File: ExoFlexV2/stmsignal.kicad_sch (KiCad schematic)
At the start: 4 parts, among them J4 CN8, J5 CN9, J6 CN7, J7 CN10

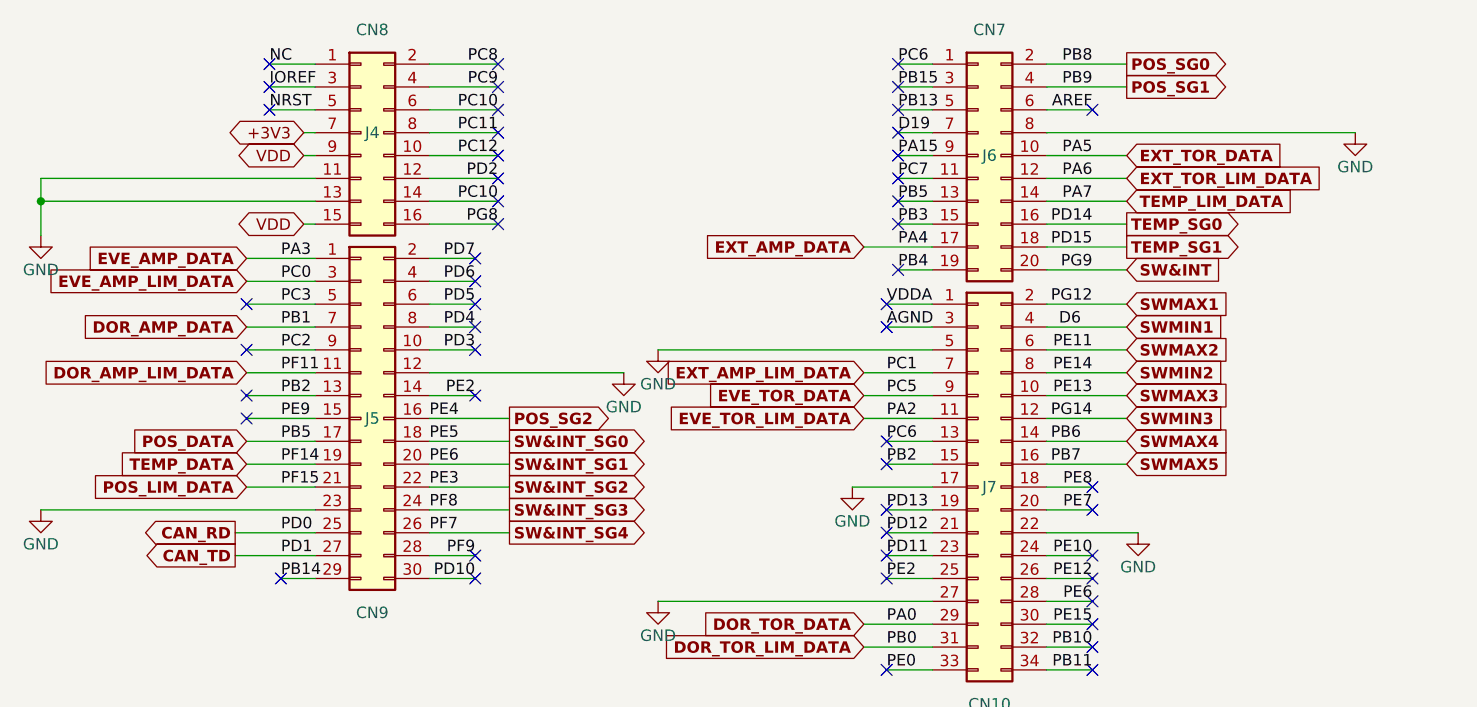
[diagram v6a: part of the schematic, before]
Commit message: Gestion de multiple signaux
- Ajout de multiplexeur 8:1 pour les signaux analogique supplémentaire
- Ajout de multiplexeur 8:1 arranger sous forme d'un 32:1
- Ajout du footprint pour le mux choisis
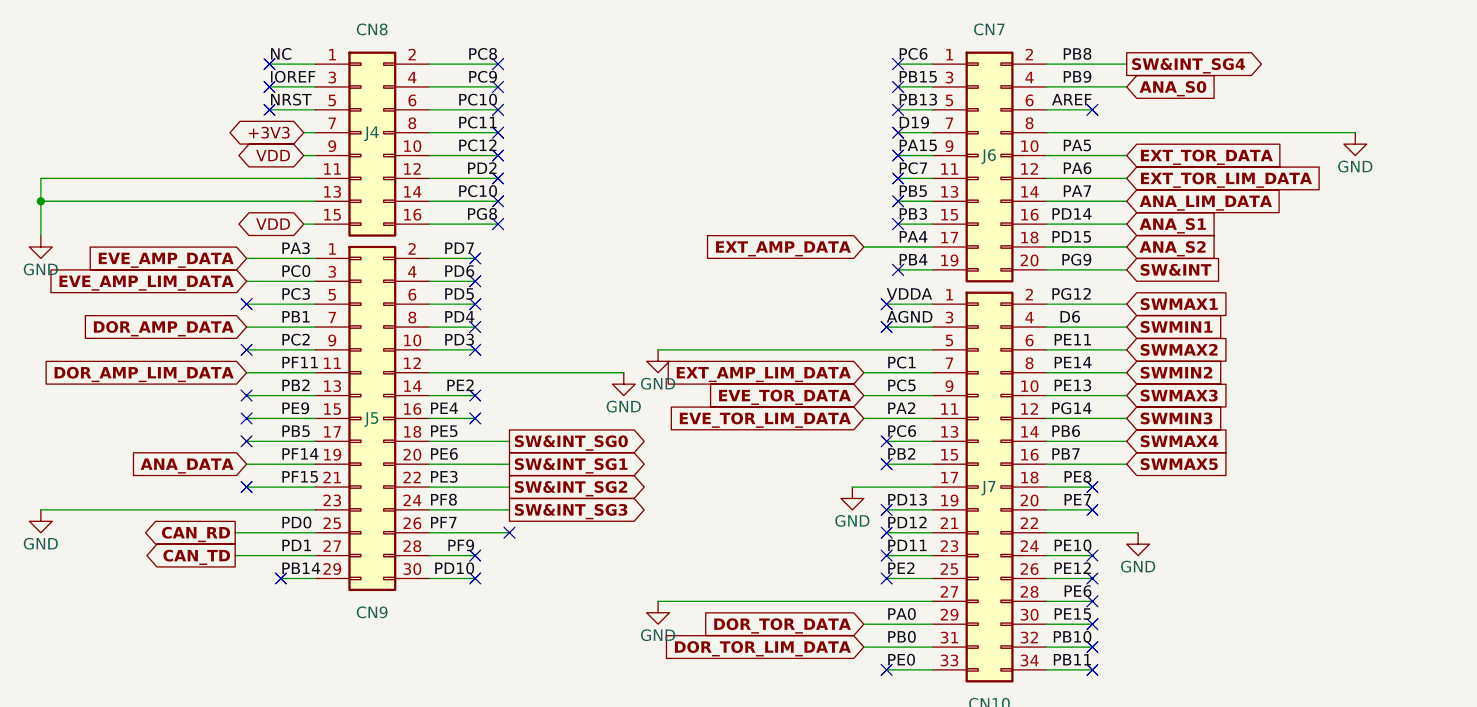
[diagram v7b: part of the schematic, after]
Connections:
- net POS_SG0 is gone; now on net SW&INT_SG4: J6.2 (Pin_2)
- net SW&INT_SG4: no longer J5.26 (Pin_26)
- net POS_DATA renamed PB5
- net POS_LIM_DATA renamed PF15
- net POS_SG1 renamed ANA_S0
- net POS_SG2 renamed PE4
- net TEMP_DATA renamed ANA_DATA
- net TEMP_LIM_DATA renamed ANA_LIM_DATA
- net TEMP_SG0 renamed ANA_S1
- net TEMP_SG1 renamed ANA_S2
- new net PF7: J5.26 (Pin_26)
- no-connect marks 51 -> 55
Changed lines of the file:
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@@
   )
   (no_connect (at 156.21 69.85))
+  (no_connect (at 83.82 101.6))
   (no_connect (at 111.76 67.31))
   (no_connect (at 86.36 54.61))
@@
   (no_connect (at 83.82 93.98))
   (no_connect (at 83.82 81.28))
+  (no_connect (at 109.22 93.98))
   (no_connect (at 111.76 54.61))
   (no_connect (at 177.8 116.84))
@@
   (no_connect (at 156.21 72.39))
   (no_connect (at 156.21 67.31))
+  (no_connect (at 113.03 106.68))
   (no_connect (at 156.21 64.77))
   (no_connect (at 154.94 109.22))
@@
   (no_connect (at 109.22 111.76))
   (no_connect (at 154.94 121.92))
+  (no_connect (at 83.82 96.52))
   (wire (pts (xy 152.4 93.98) (xy 160.02 93.98))
     (stroke (width 0.5) (type default) (color 40 35 255 1))
@@
     (stroke (width 0) (type default) (color 0 0 0 0))
   )
-  (wire (pts (xy 104.14 93.98) (xy 113.03 93.98))
-    (stroke (width 0.5) (type default) (color 255 74 249 1))
-  )
   (wire (pts (xy 86.36 57.15) (xy 91.44 57.15))
     (stroke (width 0) (type default) (color 0 0 0 0))
@@
     (stroke (width 0) (type default) (color 0 0 0 0))
   )
+  (wire (pts (xy 104.14 93.98) (xy 109.22 93.98))
+    (stroke (width 0) (type default) (color 0 0 0 0))
+  )
   (polyline (pts (xy 228.6 165.1) (xy 283.21 165.1))
     (stroke (width 1) (type solid) (color 0 0 0 0))
@@
     (property "Intersheet References" "${INTERSHEET_REFS}" (id 0) (at 127.6169 104.013 0)
       (effects (font (size 1.27 1.27) (thickness 0.254) bold) (justify left) hide)
-    )
-  )
-  (global_label "POS_LIM_DATA" (shape input) (at 83.82 101.6 180) (fields_autoplaced)
-    (effects (font (size 1.27 1.27) bold) (justify right))
-    (property "Intersheet References" "${INTERSHEET_REFS}" (id 0) (at 67.7817 101.473 0)
-      (effects (font (size 1.27 1.27) bold) (justify right) hide)
     )
   )
@@
     )
   )
+  (global_label "ANA_S0" (shape input) (at 181.61 57.15 0) (fields_autoplaced)
+    (effects (font (size 1.27 1.27) (thickness 0.254) bold) (justify left))
+    (property "Intersheet References" "${INTERSHEET_REFS}" (id 0) (at 191.2983 57.277 0)
+      (effects (font (size 1.27 1.27) (thickness 0.254) bold) (justify left) hide)
+    )
+  )
   (global_label "SW&INT_SG0" (shape output) (at 113.03 96.52 0) (fields_autoplaced)
     (effects (font (size 1.27 1.27) (thickness 0.254) bold) (justify left))
@@
     )
   )
-  (global_label "TEMP_LIM_DATA" (shape input) (at 181.61 69.85 0) (fields_autoplaced)
-    (effects (font (size 1.27 1.27) bold) (justify left))
-    (property "Intersheet References" "${INTERSHEET_REFS}" (id 0) (at 198.6764 69.723 0)
-      (effects (font (size 1.27 1.27) bold) (justify left) hide)
+  (global_label "ANA_DATA" (shape input) (at 83.82 99.06 180) (fields_autoplaced)
+    (effects (font (size 1.27 1.27) bold) (justify right))
+    (property "Intersheet References" "${INTERSHEET_REFS}" (id 0) (at 72.136 99.187 0)
+      (effects (font (size 1.27 1.27) bold) (justify right) hide)
     )
   )
@@
     )
   )
-  (global_label "POS_DATA" (shape input) (at 83.82 96.52 180) (fields_autoplaced)
-    (effects (font (size 1.27 1.27) bold) (justify right))
-    (property "Intersheet References" "${INTERSHEET_REFS}" (id 0) (at 71.8336 96.393 0)
-      (effects (font (size 1.27 1.27) bold) (justify right) hide)
-    )
-  )
   (global_label "EVE_TOR_LIM_DATA" (shape input) (at 152.4 93.98 180) (fields_autoplaced)
     (effects (font (size 1.27 1.27) bold) (justify right))
@@
     )
   )
-  (global_label "POS_SG0" (shape output) (at 181.61 54.61 0) (fields_autoplaced)
-    (effects (font (size 1.27 1.27) (thickness 0.254) bold) (justify left))
-    (property "Intersheet References" "${INTERSHEET_REFS}" (id 0) (at 192.8707 54.483 0)
-      (effects (font (size 1.27 1.27) (thickness 0.254) bold) (justify left) hide)
-    )
-  )
-  (global_label "TEMP_DATA" (shape input) (at 83.82 99.06 180) (fields_autoplaced)
-    (effects (font (size 1.27 1.27) bold) (justify right))
-    (property "Intersheet References" "${INTERSHEET_REFS}" (id 0) (at 70.8055 98.933 0)
-      (effects (font (size 1.27 1.27) bold) (justify right) hide)
-    )
-  )
   (global_label "SW&INT" (shape input) (at 181.61 77.47 0) (fields_autoplaced)
     (effects (font (size 1.27 1.27) (thickness 0.254) bold) (justify left))
@@
     )
   )
-  (global_label "TEMP_SG1" (shape output) (at 181.61 74.93 0) (fields_autoplaced)
-    (effects (font (size 1.27 1.27) (thickness 0.254) bold) (justify left))
-    (property "Intersheet References" "${INTERSHEET_REFS}" (id 0) (at 193.8988 74.803 0)
+  (global_label "SW&INT_SG4" (shape output) (at 181.61 54.61 0) (fields_autoplaced)
+    (effects (font (size 1.27 1.27) (thickness 0.254) bold) (justify left))
+    (property "Intersheet References" "${INTERSHEET_REFS}" (id 0) (at 196.1969 54.483 0)
       (effects (font (size 1.27 1.27) (thickness 0.254) bold) (justify left) hide)
     )
@@
     (effects (font (size 1.27 1.27) (thickness 0.254) bold) (justify left))
     (property "Intersheet References" "${INTERSHEET_REFS}" (id 0) (at 192.024 98.933 0)
-      (effects (font (size 1.27 1.27) (thickness 0.254) bold) (justify left) hide)
-    )
-  )
-  (global_label "TEMP_SG0" (shape output) (at 181.61 72.39 0) (fields_autoplaced)
-    (effects (font (size 1.27 1.27) (thickness 0.254) bold) (justify left))
-    (property "Intersheet References" "${INTERSHEET_REFS}" (id 0) (at 193.8988 72.263 0)
       (effects (font (size 1.27 1.27) (thickness 0.254) bold) (justify left) hide)
     )
@@
     )
   )
-  (global_label "POS_SG2" (shape output) (at 113.03 93.98 0) (fields_autoplaced)
-    (effects (font (size 1.27 1.27) (thickness 0.254) bold) (justify left))
-    (property "Intersheet References" "${INTERSHEET_REFS}" (id 0) (at 124.2907 93.853 0)
-      (effects (font (size 1.27 1.27) (thickness 0.254) bold) (justify left) hide)
-    )
-  )
   (global_label "SWMAX4" (shape input) (at 181.61 96.52 0) (fields_autoplaced)
     (effects (font (size 1.27 1.27) (thickness 0.254) bold) (justify left))
     (property "Intersheet References" "${INTERSHEET_REFS}" (id 0) (at 192.024 96.393 0)
+      (effects (font (size 1.27 1.27) (thickness 0.254) bold) (justify left) hide)
+    )
+  )
+  (global_label "ANA_S1" (shape input) (at 181.61 72.39 0) (fields_autoplaced)
+    (effects (font (size 1.27 1.27) (thickness 0.254) bold) (justify left))
+    (property "Intersheet References" "${INTERSHEET_REFS}" (id 0) (at 191.2983 72.517 0)
       (effects (font (size 1.27 1.27) (thickness 0.254) bold) (justify left) hide)
     )
@@
     )
   )
+  (global_label "ANA_LIM_DATA" (shape input) (at 181.61 69.85 0) (fields_autoplaced)
+    (effects (font (size 1.27 1.27) bold) (justify left))
+    (property "Intersheet References" "${INTERSHEET_REFS}" (id 0) (at 197.3459 69.723 0)
+      (effects (font (size 1.27 1.27) bold) (justify left) hide)
+    )
+  )
   (global_label "EVE_AMP_DATA" (shape input) (at 83.82 76.2 180) (fields_autoplaced)
     (effects (font (size 1.27 1.27) bold) (justify right))
@@
     )
   )
-  (global_label "POS_SG1" (shape output) (at 181.61 57.15 0) (fields_autoplaced)
-    (effects (font (size 1.27 1.27) (thickness 0.254) bold) (justify left))
-    (property "Intersheet References" "${INTERSHEET_REFS}" (id 0) (at 192.8707 57.023 0)
-      (effects (font (size 1.27 1.27) (thickness 0.254) bold) (justify left) hide)
-    )
-  )
-  (global_label "SW&INT_SG4" (shape output) (at 113.03 106.68 0) (fields_autoplaced)
-    (effects (font (size 1.27 1.27) (thickness 0.254) bold) (justify left))
-    (property "Intersheet References" "${INTERSHEET_REFS}" (id 0) (at 127.6169 106.553 0)
-      (effects (font (size 1.27 1.27) (thickness 0.254) bold) (justify left) hide)
-    )
+  (global_label "ANA_S2" (shape input) (at 181.61 74.93 0) (fields_autoplaced)
+    (effects (font (size 1.27 1.27) (thickness 0.254) bold) (justify left))
+    (property "Intersheet References" "${INTERSHEET_REFS}" (id 0) (at 191.2983 75.057 0)
+      (effects (font (size 1.27 1.27) (thickness 0.254) bold) (justify left) hide)
+    )

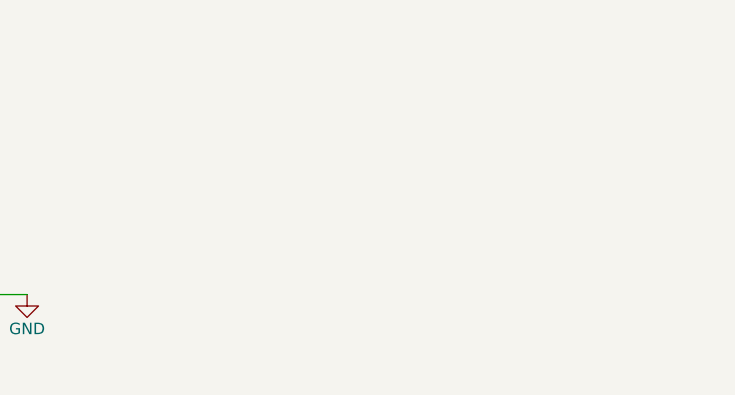
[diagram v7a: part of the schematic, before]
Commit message: Finalisation 1
- Ajout de pages pour la gestion des signaux négatif
- Modification des pages de torque et amplitude
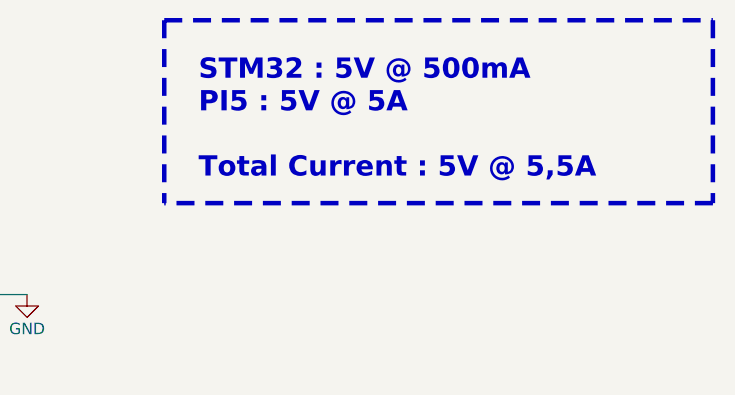
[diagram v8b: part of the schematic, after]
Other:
- note added: "STM32 : 5V @ 500mA PI5 : 5V @ 5A Total Current : 5V @ 5,5A"
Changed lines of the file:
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@@
     (stroke (width 0) (type default) (color 0 0 0 0))
+  )
+  (polyline (pts (xy 222.25 31.75) (xy 222.25 52.07))
+    (stroke (width 0.5) (type dash) (color 255 148 44 1))
+  )
+  (polyline (pts (xy 283.21 52.07) (xy 222.25 52.07))
+    (stroke (width 0.5) (type dash) (color 255 148 44 1))
   )
   (wire (pts (xy 104.14 81.28) (xy 109.22 81.28))
@@
     (stroke (width 0) (type default) (color 0 0 0 0))
   )
+  (polyline (pts (xy 283.21 31.75) (xy 283.21 52.07))
+    (stroke (width 0.5) (type dash) (color 255 148 44 1))
+  )
   (wire (pts (xy 152.4 74.93) (xy 160.02 74.93))
     (stroke (width 0.5) (type default) (color 40 35 255 1))
@@
     (stroke (width 0.5) (type default) (color 255 115 33 1))
   )
+  (polyline (pts (xy 222.25 31.75) (xy 283.21 31.75))
+    (stroke (width 0.5) (type dash) (color 255 148 44 1))
+  )
   (wire (pts (xy 104.14 78.74) (xy 109.22 78.74))
     (stroke (width 0) (type default) (color 0 0 0 0))
@@
     (stroke (width 0.5) (type default) (color 40 35 255 1))
   )
+  (text "STM32 : 5V @ 500mA\nPI5 : 5V @ 5A\n\nTotal Current : 5V @ 5,5A"
+    (at 226.06 49.53 0)
+    (effects (font (size 2.25 2.25) (thickness 0.45) bold) (justify left bottom))
+  )
   (text ": ANALOG INPUT" (at 247.65 151.13 0)
